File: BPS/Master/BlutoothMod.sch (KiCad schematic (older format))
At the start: 12 parts, among them SW2 SW_DIP_x01, U6 RN4870-V_RM118, U7 MCP100-315D

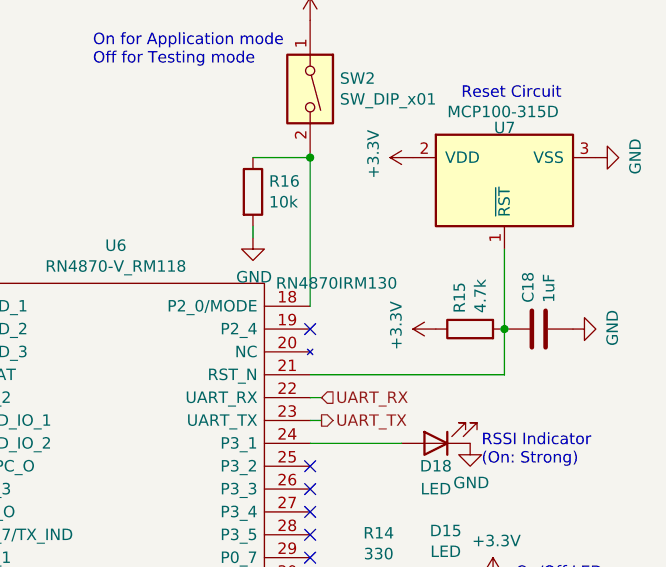
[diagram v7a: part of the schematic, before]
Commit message: Connected bluetooth module symbol to footprint and made all library paths relative.
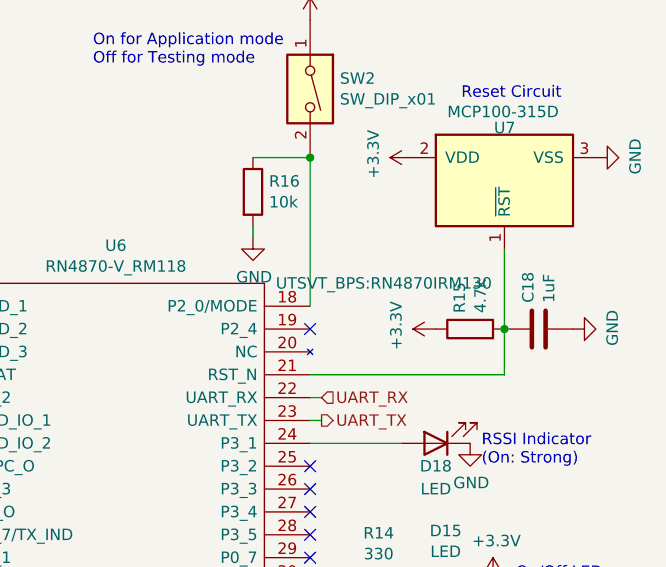
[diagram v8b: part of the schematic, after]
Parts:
- U6: footprint RN4870IRM130 -> UTSVT_BPS:RN4870IRM130
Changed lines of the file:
@@
 F 0 "U6" H 5850 3165 50  0000 C CNN
 F 1 "RN4870-V_RM118" H 5850 3074 50  0000 C CNN
-F 2 "RN4870IRM130" H 6550 3000 50  0000 L CNN
+F 2 "UTSVT_BPS:RN4870IRM130" H 6550 3000 50  0000 L CNN
 F 3 "http://docs-emea.rs-online.com/webdocs/152f/0900766b8152ff8f.pdf" H 6550 2900 50  0001 L CNN
 F 4 "Microchip RN4870-V/RM118 Bluetooth Chip 4.2" H 6550 2800 50  0001 L CNN "Description"
